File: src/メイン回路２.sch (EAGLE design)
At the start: 4 parts

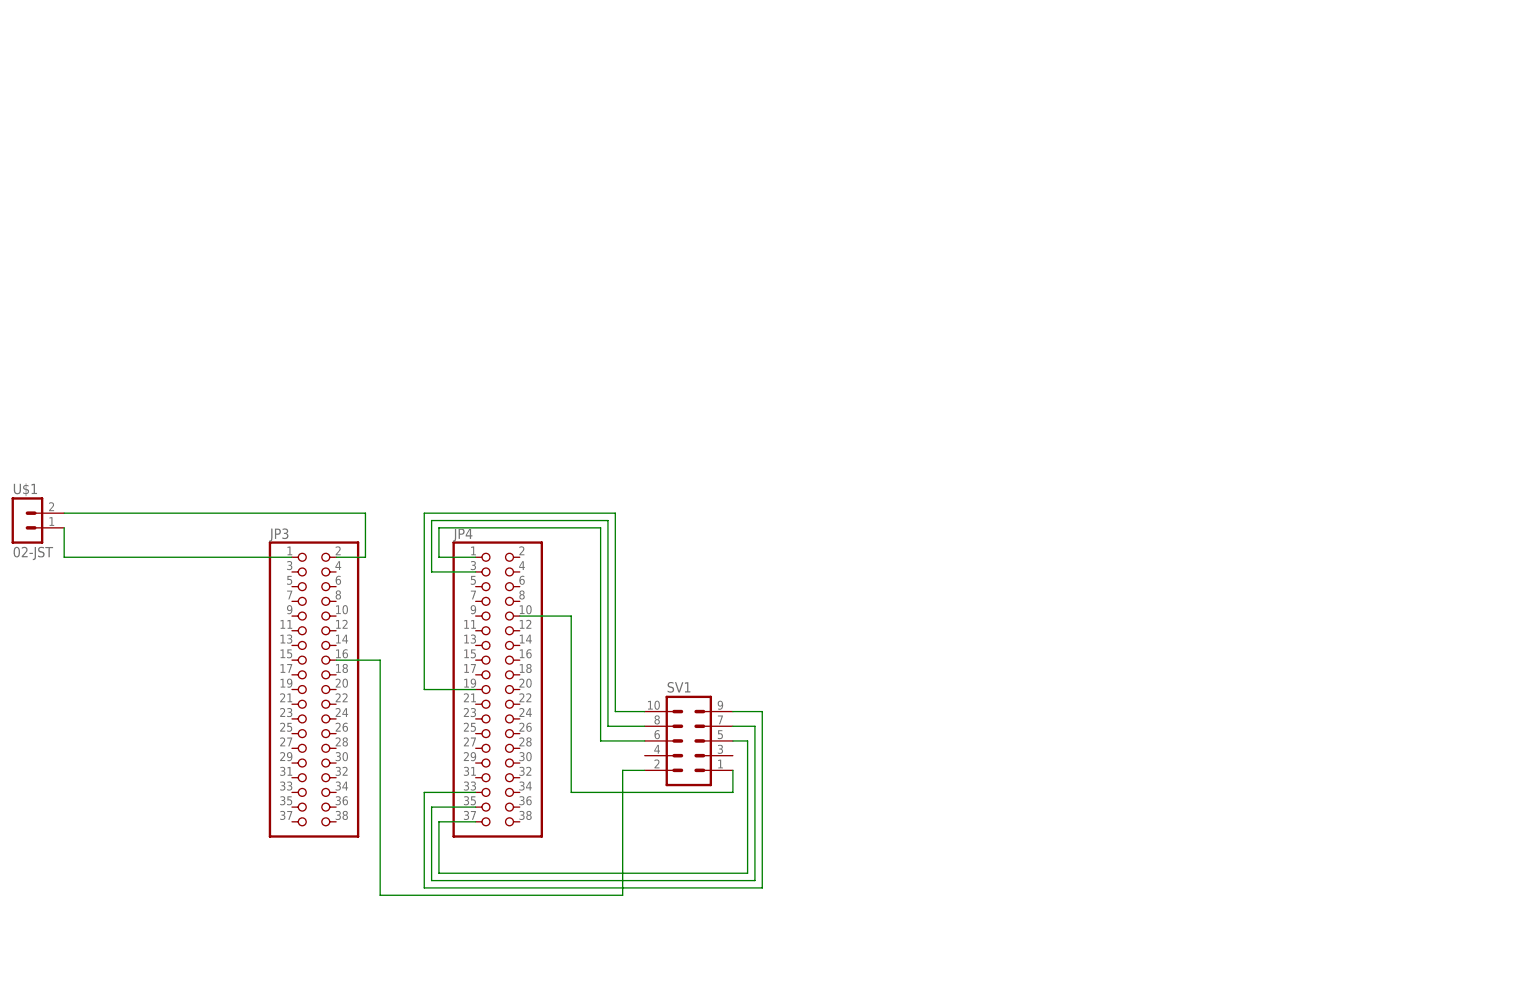
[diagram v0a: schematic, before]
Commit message: [fix]受信側の回路のsch修正全て
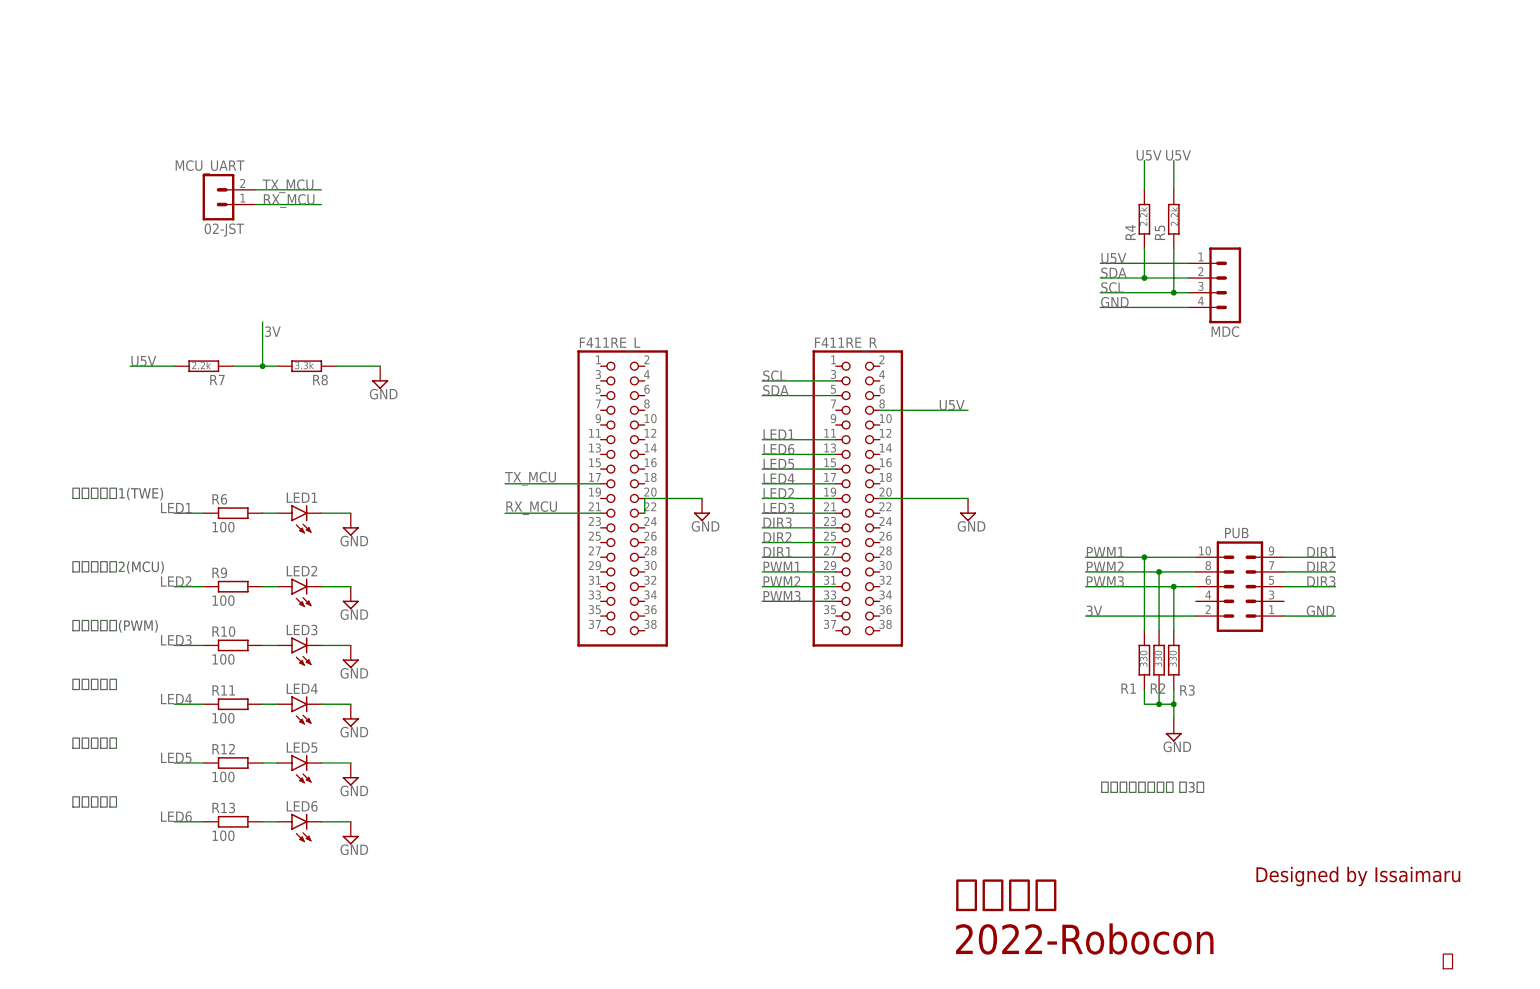
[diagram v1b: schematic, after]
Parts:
- removed JP3, JP4: (no value), pinhead:PINHD-2X19
- removed SV1: (no value), con-ml:ML10
- removed U$1: 02-JST, con-jst-xh (1):02-JST
- added F411RE_L, F411RE_R: (no value), pinhead:PINHD-2X19
- added LED1, LED2, LED3, LED4, LED5, LED6: (no value), led:LED5MM
- added MCU_UART: 02-JST, con-jst-xh (1):02-JST
- added MDC: (no value), con-jst-xh:04-JST
- added PUB: (no value), con-ml:ML10
- added R1, R2, R3: 330, rcl:R-EU_0204/7
- added R10, R11, R12, R13, R6, R9: 100, rcl:R-EU_0204/7
- added R4, R5, R7: 2.2k, rcl:R-EU_0204/7
- added R8: 3.3k, rcl:R-EU_0204/7
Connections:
- removed net N$10: JP4.10, SV1.1
- removed net N$11: JP3.16, SV1.2
- removed net N$12: JP3.2, U$1.2
- removed net N$13: JP3.1, U$1.1
- removed net N$7: JP4.35, SV1.7
- removed net N$8: JP4.33, SV1.9
- new net 3V: PUB.2, R7.1, R8.2
- new net DIR1: F411RE_R.27, PUB.9
- new net DIR2: F411RE_R.25, PUB.7
- new net DIR3: F411RE_R.23, PUB.5
- new net GND: F411RE_L.20, F411RE_L.22, F411RE_R.20, LED1.C, LED2.C, LED3.C, LED4.C, LED5.C, LED6.C, MDC.4, PUB.1, R1.1, R2.1, R3.1, R8.1
- new net LED1: F411RE_R.11, R6.1
- new net LED2: F411RE_R.19, R9.1
- new net LED3: F411RE_R.21, R10.1
- new net LED4: F411RE_R.17, R11.1
- new net LED5: F411RE_R.15, R12.1
- new net LED6: F411RE_R.13, R13.1
- new net N$1: LED2.A, R9.2
- new net N$5: LED5.A, R12.2
- new net PWM1: F411RE_R.29, PUB.10, R1.2
- new net PWM2: F411RE_R.31, PUB.8, R2.2
- new net PWM3: F411RE_R.33, PUB.6, R3.2
- new net RX_MCU: F411RE_L.21, MCU_UART.1
- new net SCL: F411RE_R.3, MDC.3, R5.1
- new net SDA: F411RE_R.5, MDC.2, R4.1
- new net TX_MCU: F411RE_L.17, MCU_UART.2
- new net U5V: F411RE_R.8, MDC.1, R4.2, R5.2, R7.2
- net N$2: now also LED1.A, R6.2; no longer JP4.1, SV1.6
- net N$3: now also LED3.A, R10.2; no longer JP4.3, SV1.8
- net N$4: now also LED4.A, R11.2; no longer JP4.19, SV1.10
- net N$6: now also LED6.A, R13.2; no longer JP4.37, SV1.5
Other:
- note added: "Designed by Issaimaru"
- note added: "上下，装填，射出 計3つ"
- note added: "上昇確認用"
- note added: "上部機構 2022-Robocon"
- note added: "下降確認用"
- note added: "受信確認用1(TWE)"
- note added: "受信確認用2(MCU)"
- note added: "完"
- note added: "射出確認用"
- note added: "速度確認用(PWM)"

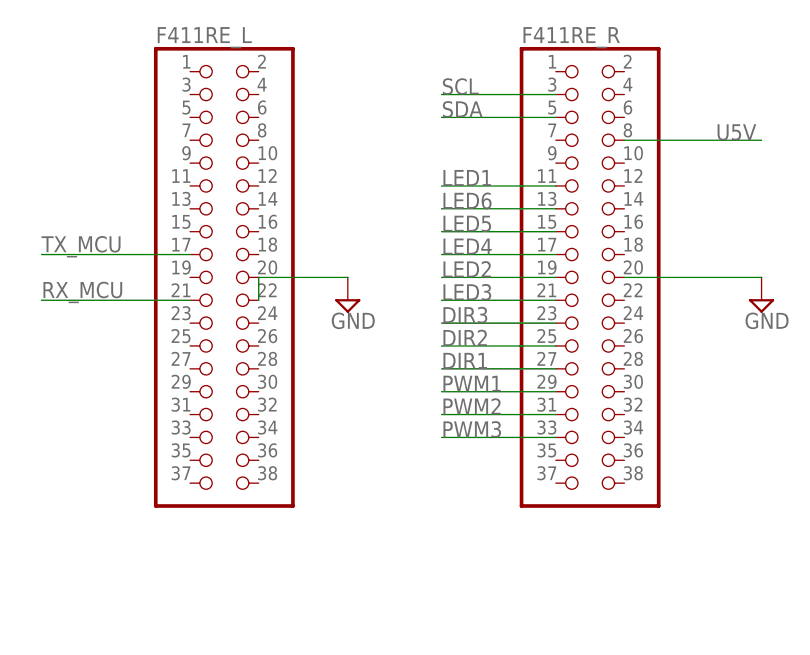
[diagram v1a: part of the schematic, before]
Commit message: [fix]brd途中まで変更
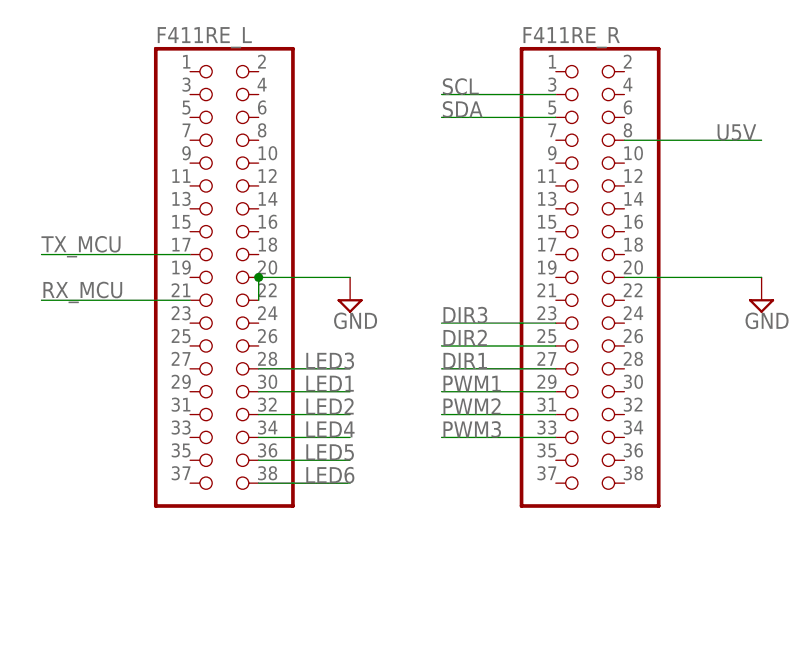
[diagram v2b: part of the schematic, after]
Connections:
- net LED1: now also F411RE_L.30; no longer F411RE_R.11
- net LED2: now also F411RE_L.32; no longer F411RE_R.19
- net LED3: now also F411RE_L.28; no longer F411RE_R.21
- net LED4: now also F411RE_L.34; no longer F411RE_R.17
- net LED5: now also F411RE_L.36; no longer F411RE_R.15
- net LED6: now also F411RE_L.38; no longer F411RE_R.13
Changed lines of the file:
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@@
 <part name="SUPPLY2" library="supply2" library_urn="urn:adsk.eagle:library:372" deviceset="GND" device=""/>
 <part name="F411RE_L" library="pinhead" library_urn="urn:adsk.eagle:library:325" deviceset="PINHD-2X19" device="" package3d_urn="urn:adsk.eagle:package:22500/2"/>
-<part name="SUPPLY6" library="supply2" library_urn="urn:adsk.eagle:library:372" deviceset="GND" device=""/>
 <part name="R6" library="rcl" library_urn="urn:adsk.eagle:library:334" deviceset="R-EU_" device="0204/7" package3d_urn="urn:adsk.eagle:package:23498/2" value="100"/>
 <part name="LED1" library="led" library_urn="urn:adsk.eagle:library:259" deviceset="LED" device="5MM" package3d_urn="urn:adsk.eagle:package:15799/2"/>
@@
 <part name="LED6" library="led" library_urn="urn:adsk.eagle:library:259" deviceset="LED" device="5MM" package3d_urn="urn:adsk.eagle:package:15799/2"/>
 <part name="SUPPLY10" library="supply2" library_urn="urn:adsk.eagle:library:372" deviceset="GND" device=""/>
+<part name="SUPPLY6" library="supply2" library_urn="urn:adsk.eagle:library:372" deviceset="GND" device=""/>
 </parts>
 <sheets>
@@
 <attribute name="VALUE" x="100.33" y="58.42" size="1.778" layer="96"/>
 </instance>
-<instance part="SUPPLY6" gate="GND" x="121.666" y="83.82" smashed="yes">
-<attribute name="VALUE" x="119.761" y="80.645" size="1.778" layer="96"/>
-</instance>
 <instance part="R6" gate="G$1" x="40.64" y="83.82" smashed="yes">
 <attribute name="NAME" x="36.83" y="85.3186" size="1.778" layer="95"/>
@@
 <instance part="SUPPLY10" gate="GND" x="60.96" y="27.94" smashed="yes">
 <attribute name="VALUE" x="59.055" y="24.765" size="1.778" layer="96"/>
+</instance>
+<instance part="SUPPLY6" gate="GND" x="121.92" y="83.82" smashed="yes">
+<attribute name="VALUE" x="120.015" y="80.645" size="1.778" layer="96"/>
 </instance>
 </instances>
@@
 </segment>
 <segment>
-<pinref part="F411RE_L" gate="G$1" pin="20"/>
-<pinref part="SUPPLY6" gate="GND" pin="GND"/>
-<pinref part="F411RE_L" gate="G$1" pin="22"/>
-<wire x1="111.76" y1="86.36" x2="121.666" y2="86.36" width="0.1524" layer="91"/>
-<wire x1="111.76" y1="83.82" x2="111.76" y2="86.36" width="0.1524" layer="91"/>
-</segment>
-<segment>
 <pinref part="LED1" gate="G$1" pin="C"/>
 <wire x1="55.88" y1="83.82" x2="60.96" y2="83.82" width="0.1524" layer="91"/>
@@
 <wire x1="55.88" y1="30.48" x2="60.96" y2="30.48" width="0.1524" layer="91"/>
 <pinref part="SUPPLY10" gate="GND" pin="GND"/>
+</segment>
+<segment>
+<pinref part="F411RE_L" gate="G$1" pin="20"/>
+<pinref part="F411RE_L" gate="G$1" pin="22"/>
+<wire x1="111.76" y1="86.36" x2="111.76" y2="83.82" width="0.1524" layer="91"/>
+<wire x1="111.76" y1="86.36" x2="121.92" y2="86.36" width="0.1524" layer="91"/>
+<junction x="111.76" y="86.36"/>
+<pinref part="SUPPLY6" gate="GND" pin="GND"/>
 </segment>
 </net>
@@
 <net name="LED1" class="0">
 <segment>
-<pinref part="F411RE_R" gate="G$1" pin="11"/>
-<wire x1="144.78" y1="96.52" x2="132.08" y2="96.52" width="0.1524" layer="91"/>
-<label x="132.08" y="96.52" size="1.778" layer="95"/>
-</segment>
-<segment>
 <wire x1="30.48" y1="83.82" x2="35.56" y2="83.82" width="0.1524" layer="91"/>
 <pinref part="R6" gate="G$1" pin="1"/>
 <label x="27.94" y="83.82" size="1.778" layer="95"/>
 </segment>
+<segment>
+<pinref part="F411RE_L" gate="G$1" pin="30"/>
+<wire x1="111.76" y1="73.66" x2="121.92" y2="73.66" width="0.1524" layer="91"/>
+<label x="116.84" y="73.66" size="1.778" layer="95"/>
+</segment>
 </net>
 <net name="N$2" class="0">
@@
 </segment>
 <segment>
-<pinref part="F411RE_R" gate="G$1" pin="19"/>
-<wire x1="144.78" y1="86.36" x2="132.08" y2="86.36" width="0.1524" layer="91"/>
-<label x="132.08" y="86.36" size="1.778" layer="95"/>
+<pinref part="F411RE_L" gate="G$1" pin="32"/>
+<wire x1="111.76" y1="71.12" x2="121.92" y2="71.12" width="0.1524" layer="91"/>
+<label x="116.84" y="71.12" size="1.778" layer="95"/>
 </segment>
 </net>
@@
 </segment>
 <segment>
-<pinref part="F411RE_R" gate="G$1" pin="21"/>
-<wire x1="144.78" y1="83.82" x2="132.08" y2="83.82" width="0.1524" layer="91"/>
-<label x="132.08" y="83.82" size="1.778" layer="95"/>
+<pinref part="F411RE_L" gate="G$1" pin="28"/>
+<wire x1="111.76" y1="76.2" x2="121.92" y2="76.2" width="0.1524" layer="91"/>
+<label x="116.84" y="76.2" size="1.778" layer="95"/>
 </segment>
 </net>
@@
 </segment>
 <segment>
-<pinref part="F411RE_R" gate="G$1" pin="17"/>
-<wire x1="144.78" y1="88.9" x2="132.08" y2="88.9" width="0.1524" layer="91"/>
-<label x="132.08" y="88.9" size="1.778" layer="95"/>
+<pinref part="F411RE_L" gate="G$1" pin="34"/>
+<wire x1="111.76" y1="68.58" x2="121.92" y2="68.58" width="0.1524" layer="91"/>
+<label x="116.84" y="68.58" size="1.778" layer="95"/>
 </segment>
 </net>
@@
 </segment>
 <segment>
-<pinref part="F411RE_R" gate="G$1" pin="15"/>
-<wire x1="144.78" y1="91.44" x2="132.08" y2="91.44" width="0.1524" layer="91"/>
-<label x="132.08" y="91.44" size="1.778" layer="95"/>
+<pinref part="F411RE_L" gate="G$1" pin="36"/>
+<wire x1="111.76" y1="66.04" x2="121.92" y2="66.04" width="0.1524" layer="91"/>
+<label x="116.84" y="66.04" size="1.778" layer="95"/>
 </segment>
 </net>
@@
 </segment>
 <segment>
-<pinref part="F411RE_R" gate="G$1" pin="13"/>
-<wire x1="144.78" y1="93.98" x2="132.08" y2="93.98" width="0.1524" layer="91"/>
-<label x="132.08" y="93.98" size="1.778" layer="95"/>
-</segment>
-</net>
+<pinref part="F411RE_L" gate="G$1" pin="38"/>
+<wire x1="111.76" y1="63.5" x2="121.92" y2="63.5" width="0.1524" layer="91"/>
+<label x="116.84" y="63.5" size="1.778" layer="95"/>
+</segment>
+</net>

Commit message: [complete]メイン回路2の完成
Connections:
- net GND: now also PUB.3, PUB.4
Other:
- note added: "受信確認用1(MDC)"
- note removed: "受信確認用1(TWE)"
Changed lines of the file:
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@@
 <text x="217.17" y="20.066" size="2.54" layer="94">Designed by Issaimaru</text>
 <text x="249.428" y="5.08" size="2.54" layer="94">完</text>
-<text x="12.7" y="86.36" size="1.778" layer="97">受信確認用1(TWE)</text>
+<text x="12.7" y="86.36" size="1.778" layer="97">受信確認用1(MDC)</text>
 <text x="12.7" y="73.66" size="1.778" layer="97">受信確認用2(MCU)</text>
 <text x="12.7" y="63.5" size="1.778" layer="97">速度確認用(PWM)</text>
@@
 <pinref part="SUPPLY6" gate="GND" pin="GND"/>
 </segment>
+<segment>
+<pinref part="PUB" gate="G$1" pin="4"/>
+<wire x1="207.01" y1="68.58" x2="187.96" y2="68.58" width="0.1524" layer="91"/>
+<label x="187.96" y="68.58" size="1.778" layer="95"/>
+</segment>
+<segment>
+<pinref part="PUB" gate="G$1" pin="3"/>
+<wire x1="222.25" y1="68.58" x2="231.14" y2="68.58" width="0.1524" layer="91"/>
+<label x="226.06" y="68.58" size="1.778" layer="95"/>
+</segment>
 </net>
